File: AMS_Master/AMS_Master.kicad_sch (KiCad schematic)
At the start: 13 parts, among them IC1 LTM2884CY#PBF, IC2 LTC4411ES5#TRMPBF, IC3 ISO1042DWVR, J1 Conn_01x04_Socket, J2 Conn_01x04_Socket, J3 USB_B, U1 LD1117S50TR_SOT223, U2 ADuM1250, U3 MCP2515-xSO, Y1 Crystal

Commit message: AMS_Master更新
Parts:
- added C10, C11, C12, C3, C4, C5, C6, C7, C8, C9: C, symbol Device:C
- added D1, D2, D3: LED, symbol Device:LED
- added R1, R2, R3, R4, R5, R6, R7, R8: R, symbol Device:R
- added U4: ATmega328P-A, Package_QFP:TQFP-32_7x7mm_P0.8mm, symbol MCU_Microchip_ATmega:ATmega328P-A
- added U5: FT232RL, Package_SO:SSOP-28_5.3x10.2mm_P0.65mm, symbol Interface_USB:FT232RL
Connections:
- net GND1: now reaches U1.1 (GND)
- net GND1: now also IC1.A3 (SPND-_PWR), IC1.A6 (GND_1), IC1.B1 (GND_2), IC1.B10 (GND_11), IC1.B11 (GND_12), IC1.B2 (GND_3), IC1.B3 (GND_4), IC1.B4 (GND_5), IC1.B5 (GND_6), IC1.B6 (GND_7), IC1.B7 (GND_8), IC1.B8 (GND_9), IC1.B9 (GND_10), J1.1 (Pin_1), J2.4 (Pin_4), C11.2, C12.2, C3.2, C4.1, R1.2
- net +5V: now reaches U1.2 (VO)
- net +5V: now also C12.1, C6.1, R5.2, R6.2, R7.2, R8.2, U5.19 (~{RESET}), U5.20 (VCC), U5.4 (VCCIO)
- net +12V: now reaches U1.3 (VI)
- net +12V: now also J1.4 (Pin_4), J2.1 (Pin_1), C11.1
- net at IC1.A1 (D1-): now also J3.2 (D-)
- net at IC1.A10 (VCC_3): now also IC1.A11 (VCC_4), IC1.A7 (VBUS), IC1.A8 (VCC_1), IC1.A9 (VCC_2), J3.1 (VBUS)
- net at IC1.A2 (D1+): now also J3.3 (D+)
- net at IC1.A4 (ON): now also IC1.A5 (VLO)
- net GND: now reaches IC1.K1 (GND2_1)
- net GND: now also IC1.K10 (GND2_10), IC1.K11 (GND2_11), IC1.K2 (GND2_2), IC1.K3 (GND2_3), IC1.K4 (GND2_4), IC1.K5 (GND2_5), IC1.K6 (GND2_6), IC1.K7 (GND2_7), IC1.K8 (GND2_8), IC1.K9 (GND2_9), IC1.L3 (GND2_12), IC1.L4 (GND2_13), IC1.L6 (GND2_14), IC1.L7 (GND2_15), C5.2, C6.2, C7.2, D3.1 (K), R4.1, U5.18 (GND), U5.21 (GND), U5.25 (AGND), U5.26 (TEST), U5.7 (GND)
- net at IC1.L1 (D2-): now also U5.16 (USBD-)
- net at IC1.L10 (VCC2_3): now also IC1.L11 (VCC2_4), IC1.L8 (VCC2_1), IC1.L9 (VCC2_2), IC2.1 (IN)
- net at IC1.L2 (D2+): now also U5.15 (USBD+)
- net at J3.5 (Shield): now also C3.1, R1.1
- new net: C4.2, C5.1
- new net: C8.2, R5.1
- new net: D3.2 (A), R8.1
- new net: C8.1, R4.2, U5.2 (DTR)
- new net: R3.1, U5.5 (RXD)
- new net: C7.1, U5.17 (3V3OUT)
- new net: D1.1 (K), U5.23 (CBUS0)
- new net: D1.2 (A), R6.1
- new net: D2.2 (A), R7.1
- new net: U4.21 (GND), U4.3 (GND), U4.5 (GND)
- new net: U4.4 (VCC), U4.6 (VCC)
- new net: R2.1, U5.1 (TXD)
- new net: D2.1 (K), U5.22 (CBUS1)
- no-connect marks 0 -> 11
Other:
- moved on the sheet: C1, C2, IC1, IC2, J1, J2, J3, PS1, U1, U2, U3, Y1

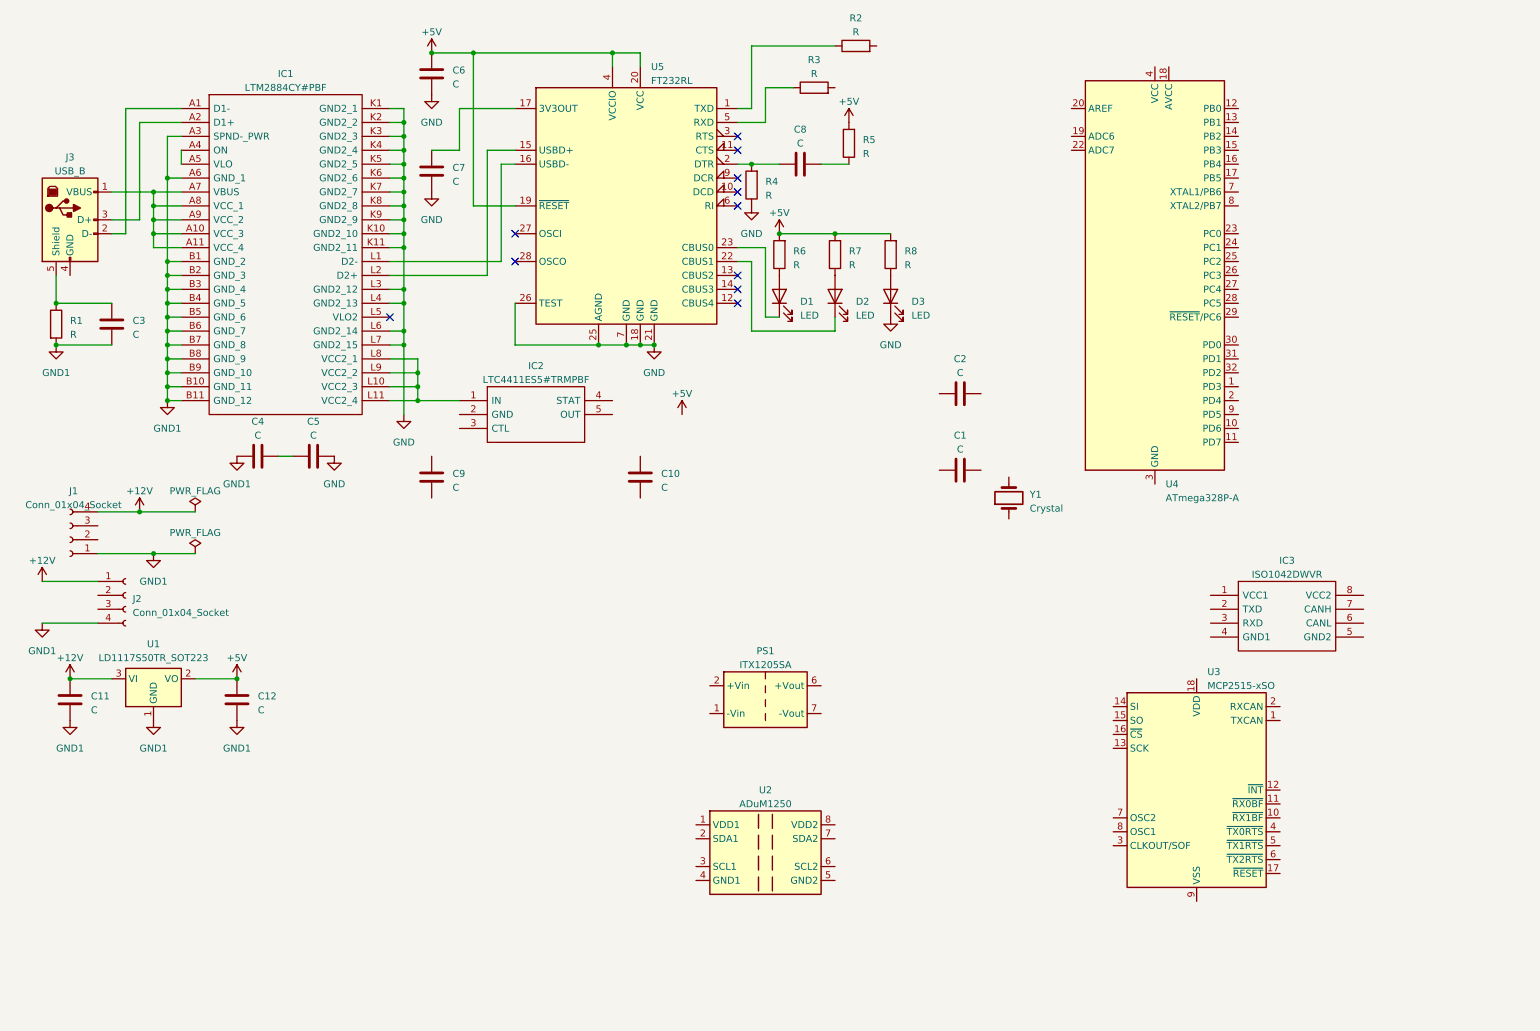
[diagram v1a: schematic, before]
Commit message: AMS_Master回路図作成
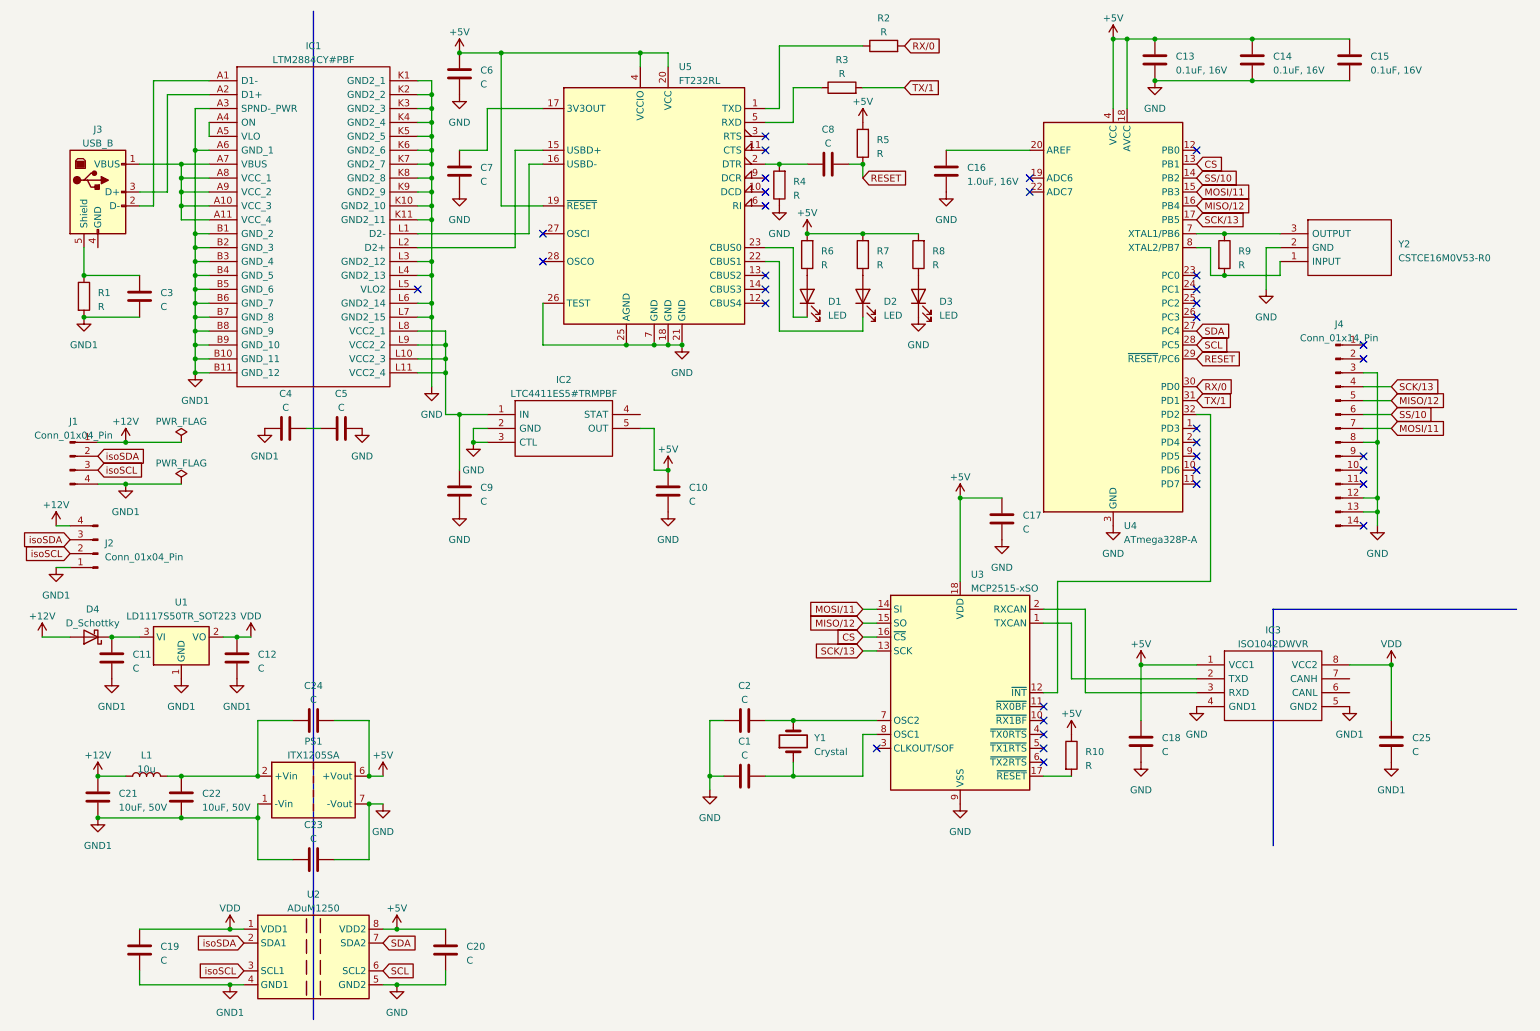
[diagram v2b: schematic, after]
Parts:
- removed J1, J2: Conn_01x04_Socket, Connector_JST:JST_XH_S4B-XH-A_1x04_P2.50mm_Horizontal, symbol Connector:Conn_01x04_Socket
- added C13, C14, C15: 0.1uF, 16V, symbol Device:C
- added C16: 1.0uF, 16V, symbol Device:C
- added C17, C18, C19, C20, C23, C24, C25: C, symbol Device:C
- added C21, C22: 10uF, 50V, symbol Device:C
- added D4: D_Schottky, SamacSys_Parts:CUHS20S40H3F, symbol Device:D_Schottky
- added J1, J2: Conn_01x04_Pin, Connector_JST:JST_XH_S4B-XH-A_1x04_P2.50mm_Horizontal, symbol Connector:Conn_01x04_Pin
- added J4: Conn_01x14_Pin, SamacSys_Parts:SHDR14W55P200_2X7_1665X630X640P, symbol Connector:Conn_01x14_Pin
- added L1: 10u, symbol Device:L
- added R10, R9: R, symbol Device:R
- added Y2: CSTCE16M0V53-R0, CSTCE16M0V53R0, symbol SamacSys_Parts:CSTCE16M0V53-R0
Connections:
- net +12V: now also C21.1, D4.2 (A), J1.1 (Pin_1), J2.4 (Pin_4), L1.1; no longer C11.1, U1.3 (VI)
- net +5V: now also C10.1, IC2.5 (OUT), IC3.1 (VCC1), PS1.6 (+Vout), U2.8 (VDD2), U3.18 (VDD), U4.18 (AVCC), U4.4 (VCC), U4.6 (VCC), C13.1, C14.1, C15.1, C17.2, C18.1, C20.1, C24.2, R10.1; no longer C12.1, U1.2 (VO)
- net GND: now also C1.1, C10.2, C2.1, C9.2, IC2.2 (GND), IC2.3 (CTL), IC3.4 (GND1), PS1.7 (-Vout), U2.5 (GND2), U3.9 (VSS), U4.21 (GND), U4.3 (GND), U4.5 (GND), C13.2, C14.2, C15.2, C16.2, C17.1, C18.2, C20.2, C23.2, J4.12 (Pin_12), J4.13 (Pin_13), J4.3 (Pin_3), J4.8 (Pin_8), Y2.2 (GND)
- net GND1: now also IC3.5 (GND2), PS1.1 (-Vin), U2.4 (GND1), C19.2, C21.2, C22.2, C23.1, C25.2, J1.4 (Pin_4), J2.1 (Pin_1)
- net at Y1.1: now also C1.2, U3.8 (OSC1)
- net at Y1.2: now also C2.2, U3.7 (OSC2)
- net at IC3.2 (TXD): now also U3.1 (TXCAN)
- net at IC3.3 (RXD): now also U3.2 (RXCAN)
- net VDD: now reaches IC3.8 (VCC2)
- net VDD: now also C12.1, U1.2 (VO), U2.1 (VDD1), C19.1, C25.1
- net RESET: now reaches C8.2, R5.1
- net RESET: now also U4.29 (~{RESET}/PC6)
- net at IC1.L10 (VCC2_3), IC1.L11 (VCC2_4), IC1.L8 (VCC2_1)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: now also C9.1
- net TX/1: now reaches R3.2
- net TX/1: now also U4.31 (PD1)
- net at U3.12 (~{INT}): now also U4.32 (PD2)
- net SCK/13: now reaches U3.13 (SCK)
- net SCK/13: now also U4.17 (PB5), J4.4 (Pin_4)
- net MOSI/11: now reaches U3.14 (SI)
- net MOSI/11: now also U4.15 (PB3), J4.7 (Pin_7)
- net MISO/12: now reaches U3.15 (SO)
- net MISO/12: now also U4.16 (PB4), J4.5 (Pin_5)
- net CS: now reaches U3.16 (~{CS})
- net CS: now also U4.13 (PB1)
- net at U3.17 (~{RESET}): now also R10.2
- net at PS1.2 (+Vin): now also C22.1, C24.1, L1.2
- net isoSDA: now reaches U2.2 (SDA1)
- net isoSDA: now also J1.2 (Pin_2), J2.3 (Pin_3)
- net isoSCL: now reaches U2.3 (SCL1)
- net isoSCL: now also J1.3 (Pin_3), J2.2 (Pin_2)
- net SCL: now reaches U2.6 (SCL2)
- net SCL: now also U4.28 (PC5)
- net SDA: now reaches U2.7 (SDA2)
- net SDA: now also U4.27 (PC4)
- net SS/10: now reaches U4.14 (PB2)
- net SS/10: now also J4.6 (Pin_6)
- net at U4.20 (AREF): now also C16.1
- net RX/0: now reaches U4.30 (PD0)
- net RX/0: now also R2.2
- net at U4.7 (XTAL1/PB6): now also R9.1, Y2.3 (OUTPUT)
- net at U4.8 (XTAL2/PB7): now also R9.2, Y2.1 (INPUT)
- new net: C11.1, D4.1 (K), U1.3 (VI)
- no-connect marks 11 -> 35
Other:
- moved on the sheet: C1, C10, C11, C12, C2, C3, C4, C5, C6, C7, C8, C9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

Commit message: AMS_Master回路図更新
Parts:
- removed C19, C20, C25, C4, C5: C, symbol Device:C
- removed IC1: LTM2884CY#PBF, BGA44C127P11X11_1500X1500X522, symbol SamacSys_Parts:LTM2884CY#PBF
- removed IC3: ISO1042DWVR, SOIC127P1150X280-8N, symbol SamacSys_Parts:ISO1042DWVR
- removed U2: ADuM1250, Package_SO:SOIC-8_3.9x4.9mm_P1.27mm, symbol Isolator:ADuM1250
- added D5: NUP2105L, Package_TO_SOT_SMD:SOT-23, symbol Power_Protection:NUP2105L
- added R11: R, symbol Device:R
- added U2: ADuM3153, Package_SO:SSOP-20_5.3x7.2mm_P0.65mm, symbol Isolator:ADuM3153
- added U6: MCP2551-I-SN, Package_SO:SOIC-8_3.9x4.9mm_P1.27mm, symbol Interface_CAN_LIN:MCP2551-I-SN
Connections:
- net VDD is gone; now on net +5V: C12.1, U1.2 (VO)
- net isoSCL is gone; now on net SCL: J1.3 (Pin_3), J2.2 (Pin_2)
- net isoSDA is gone; now on net SDA: J1.2 (Pin_2), J2.3 (Pin_3)
- net +5V: now also U2.1 (V_{DD1}), U6.3 (VDD); no longer C24.2, PS1.6 (+Vout)
- net GND: now also C11.2, C12.2, C21.2, C22.2, C23.1, C3.2, J1.4 (Pin_4), J2.1 (Pin_1), PS1.1 (-Vin), R1.2, U1.1 (GND), D5.3 (A), R11.2, U2.10 (GND_{1}), U2.2 (GND_{1}), U6.2 (VSS); no longer C23.2, J4.12 (Pin_12), J4.13 (Pin_13), J4.3 (Pin_3), J4.8 (Pin_8), PS1.7 (-Vout)
- net GND1: now also C23.2, J4.12 (Pin_12), J4.13 (Pin_13), J4.3 (Pin_3), J4.8 (Pin_8), PS1.7 (-Vout), U2.11 (GND_{2}), U2.19 (GND_{2}); no longer C11.2, C12.2, C21.2, C22.2, C23.1, C3.2, J1.4 (Pin_4), J2.1 (Pin_1), PS1.1 (-Vin), R1.2, U1.1 (GND)
- net MISO/12: now also U2.5 (MI); no longer J4.5 (Pin_5)
- net MOSI/11: now also U2.4 (MO); no longer J4.7 (Pin_7)
- net SCK/13: now also U2.3 (MCLK); no longer J4.4 (Pin_4)
- net SS/10: now also U2.6 (~{MSS}); no longer J4.6 (Pin_6)
- net at U3.1 (TXCAN): now also U6.1 (TXD)
- net at U3.2 (RXCAN): now also U6.4 (RXD)
- net USBD-: now reaches J3.2 (D-)
- net USBD-: now also U5.16 (USBD-)
- net at J3.1 (VBUS): now also C9.1, IC2.1 (IN)
- net USBD+: now reaches J3.3 (D+)
- net USBD+: now also U5.15 (USBD+)
- new net: R11.1, U6.8 (Rs)
- new net +5VD: C24.2, PS1.6 (+Vout), U2.20 (V_{DD2})
- new net isoMISO: J4.5 (Pin_5), U2.16 (SO)
- new net isoMOSI: J4.7 (Pin_7), U2.17 (SI)
- new net isoSCK: J4.4 (Pin_4), U2.18 (SCLK)
- new net isoSS: J4.6 (Pin_6), U2.15 (~{SSS})
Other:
- moved on the sheet: C1, C10, C11, C12, C13, C14, C15, C16, C17, C18, C2, C21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

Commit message: 回路図更新
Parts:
- added J5: Conn_01x02_Pin, symbol Connector:Conn_01x02_Pin
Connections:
- net CANL: now reaches U6.6 (CANL)
- net CANL: now also D5.2 (K), J5.2 (Pin_2)
- net CANH: now reaches U6.7 (CANH)
- net CANH: now also D5.1 (K), J5.1 (Pin_1)
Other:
- moved on the sheet: C1, C17, C18, C2, C21, C22, C23, C24, D5, J4, L1, PS1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

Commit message: 回路図更新
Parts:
- removed C1, C10, C2, C6, C7, C8, C9: C, symbol Device:C
- removed D2, D3: LED, symbol Device:LED
- removed IC2: LTC4411ES5#TRMPBF, SOT95P280X100-5N, symbol SamacSys_Parts:LTC4411ES5#TRMPBF
- removed J3: USB_B, symbol Connector:USB_B
- removed R6, R7, R8: R, symbol Device:R
- removed U5: FT232RL, Package_SO:SSOP-28_5.3x10.2mm_P0.65mm, symbol Interface_USB:FT232RL
- removed Y1: Crystal, symbol Device:Crystal
- added C4, C5: C, symbol Device:C
- added J3: Conn_01x06_Socket, symbol Connector:Conn_01x06_Socket
- added J6: Conn_01x04_Socket, symbol Connector:Conn_01x04_Socket
- added Y3: CSTCE16M0V53-R0, CSTCE16M0V53R0, symbol SamacSys_Parts:CSTCE16M0V53-R0
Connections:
- net +5V: now also C3.1, R4.1, J3.3 (Pin_3); no longer R5.2
- net +5VD: now also R1.1, R2.1, C4.1
- net GND: now also J3.1 (Pin_1), J3.2 (Pin_2), Y3.2 (GND); no longer R1.2, R4.1
- net GND1: now also C4.2
- net MISO/12: now also J6.4 (Pin_4)
- net MOSI/11: now also J6.3 (Pin_3)
- net RESET: now also R4.2, C5.1, J6.1 (Pin_1); no longer R5.1
- net RX/0: now also J3.4 (Pin_4); no longer R2.2
- net SCK/13: now also R3.1, J6.2 (Pin_2)
- net TX/1: now also J3.5 (Pin_5); no longer R3.2
- net isoMISO: now also R1.2
- net isoMOSI: now also R2.2
- net at U3.8 (OSC1): now also R5.2, Y3.3 (OUTPUT)
- net at U3.7 (OSC2): now also R5.1, Y3.1 (INPUT)
- net Vin: now reaches C22.1, C24.1, L1.2, PS1.2 (+Vin)
- net TXCAN: now reaches U3.1 (TXCAN), U6.1 (TXD)
- net INT: now reaches U3.12 (~{INT}), U4.32 (PD2)
- net RXCAN: now reaches U3.2 (RXCAN), U6.4 (RXD)
- net at D1.2 (A): now also R3.2
- new net DTR: C5.2, J3.6 (Pin_6)
- no-connect marks 35 -> 31
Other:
- moved on the sheet: C11, C12, C13, C14, C15, C16, C17, C18, C21, C22, C23, C24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

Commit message: AMS_Master
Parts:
- removed R9: R, symbol Device:R
- added D2: LED_R, Diode_SMD:D_0603_1608Metric, symbol Device:LED
- C11, C17, C18, C3, C4, C5: value C -> 0.1u; footprint (none) -> Capacitor_SMD:C_0603_1608Metric
- C12: value C -> 10u; footprint (none) -> Capacitor_SMD:C_0603_1608Metric
- C13, C14, C15: value 0.1uF, 16V -> 0.1u; footprint (none) -> Capacitor_SMD:C_0603_1608Metric
- C16: value 1.0uF, 16V -> 10u; footprint (none) -> Capacitor_SMD:C_0603_1608Metric
- C21, C22: value 10uF, 50V -> 10u; footprint (none) -> Capacitor_SMD:C_0603_1608Metric
- C23, C24: value C -> 220pF, 3kV
- D1: value LED -> LED_G; footprint (none) -> Diode_SMD:D_0603_1608Metric
- D4: value D_Schottky -> CUHS20S30
- J3: footprint (none) -> Connector_PinSocket_2.54mm:PinSocket_1x06_P2.54mm_Horizontal
- J6: footprint (none) -> Connector_PinSocket_2.54mm:PinSocket_1x04_P2.54mm_Horizontal
- R1, R2: value R -> 5k
- R10, R4, R5: value R -> 10k; footprint (none) -> Resistor_SMD:R_0805_2012Metric
- R11: value R -> 17k
- R3: value R -> 300; footprint (none) -> Resistor_SMD:R_0603_1608Metric
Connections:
- net +5V: now also R5.1
- net GND: now also D1.1 (K), D2.1 (K)
- net at U3.7 (OSC2), Y3.1 (INPUT): no longer R5.1
- net at U3.8 (OSC1), Y3.3 (OUTPUT): no longer R5.2
- new net: D2.2 (A), R5.2
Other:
- moved on the sheet: C14, C15, C16, D1, D4, R3, Y3
